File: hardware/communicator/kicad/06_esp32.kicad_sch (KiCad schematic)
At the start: 5 parts, among them U11 ESP32-S3-MINI-1-N4R2

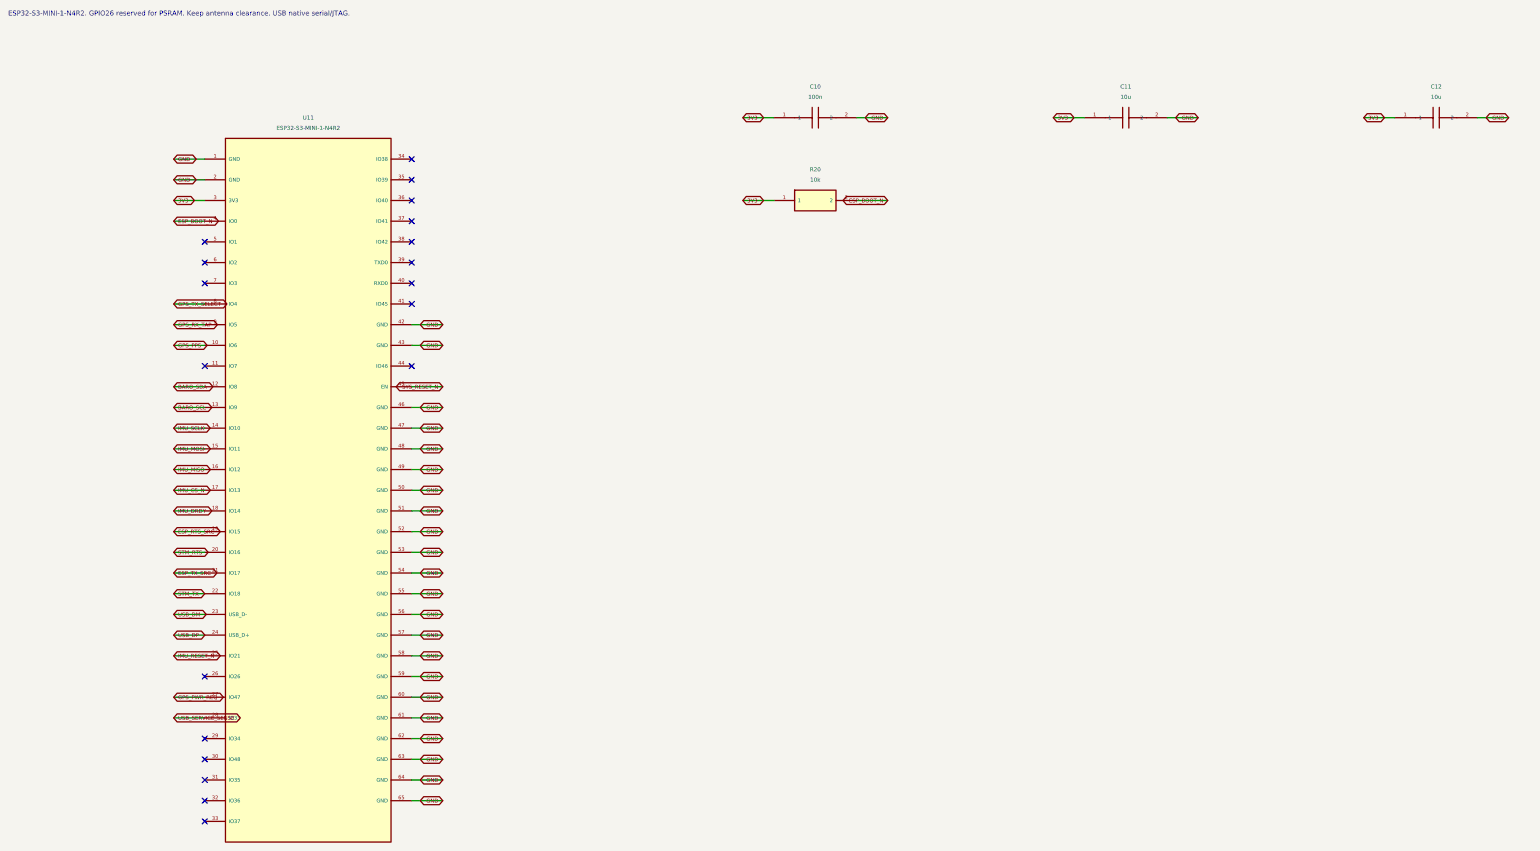
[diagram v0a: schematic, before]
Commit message: feat: add R1 detailed hardware and navigation protocol review candidate
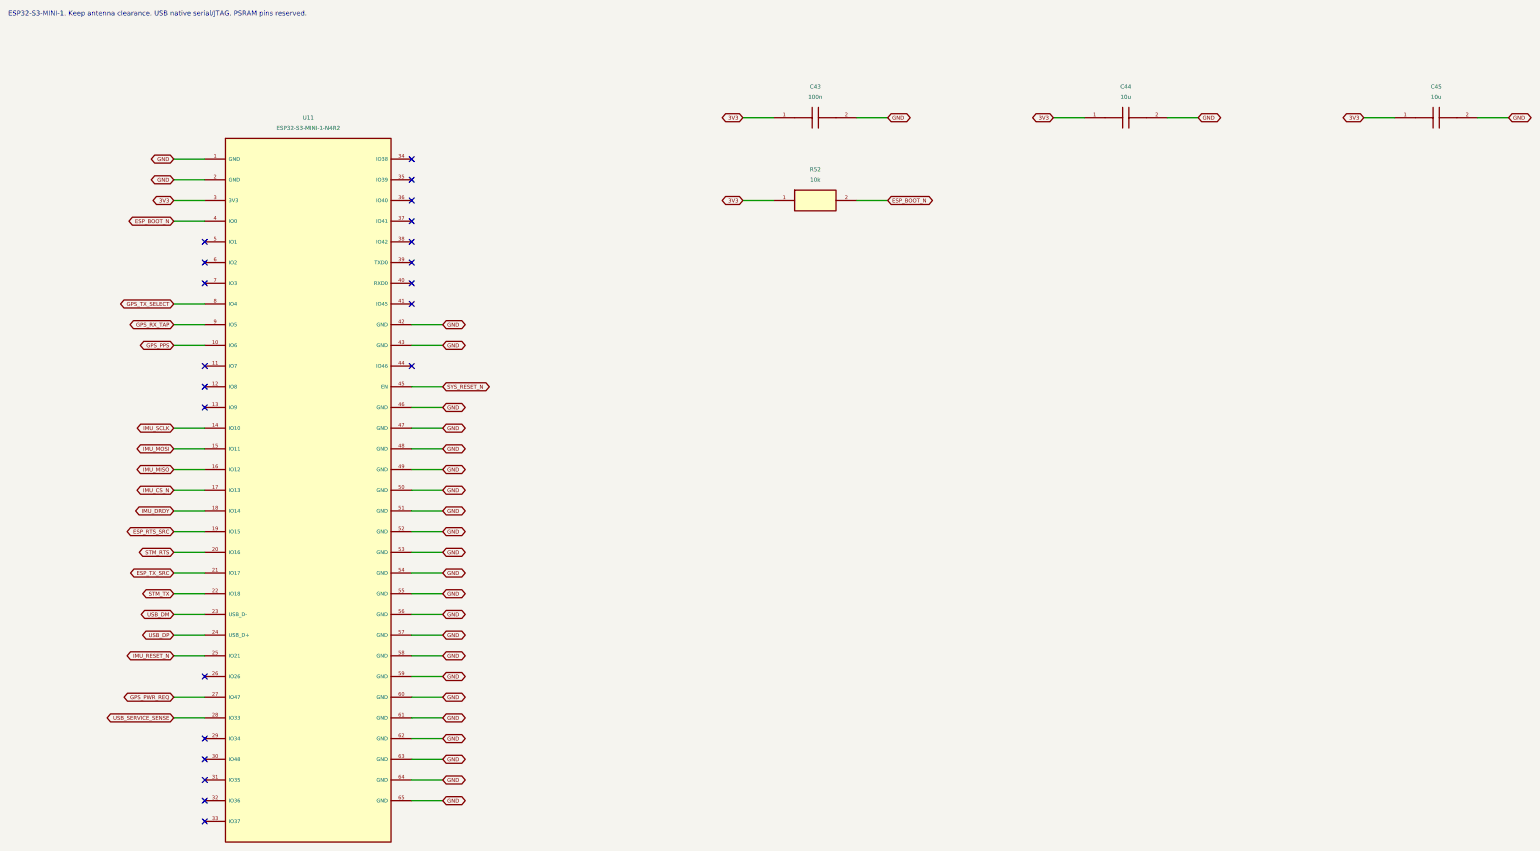
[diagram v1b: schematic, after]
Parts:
- removed C10: 100n, CANView:Capacitor_SMD__C_0603_1608Metric, symbol CANView:CANView_communicator_C10
- removed C11: 10u, CANView:Capacitor_SMD__C_0603_1608Metric, symbol CANView:CANView_communicator_C11
- removed C12: 10u, CANView:Capacitor_SMD__C_0603_1608Metric, symbol CANView:CANView_communicator_C12
- removed R20: 10k, CANView:Resistor_SMD__R_0402_1005Metric, symbol CANView:CANView_communicator_R20
- added C43: 100n, CANView:Capacitor_SMD__C_0603_1608Metric, symbol CANView:CANView_communicator_C43
- added C44: 10u, CANView:Capacitor_SMD__C_0603_1608Metric, symbol CANView:CANView_communicator_C44
- added C45: 10u, CANView:Capacitor_SMD__C_0603_1608Metric, symbol CANView:CANView_communicator_C45
- added R52: 10k, CANView:Resistor_SMD__R_0402_1005Metric, symbol CANView:CANView_communicator_R52
- U11: footprint CANView:RF_Module__ESP32-S2-MINI-1 -> CANView:ESP32-S3-MINI-1; Source esp32s3-mini: pin table, peripheral schematic and land patt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 -> esp32s3-mini
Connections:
- net 3V3: now also C43.1, C44.1, C45.1, R52.1
- net ESP_BOOT_N: now also R52.2
- net GND: now also C43.2, C44.2, C45.2
- net BARO_SCL: no longer names the net of U11.13 (IO9)
- net BARO_SDA: no longer names the net of U11.12 (IO8)
- no-connect marks 19 -> 21
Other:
- note added: "ESP32-S3-MINI-1. Keep antenna clearance. USB native serial/JTAG. PSRAM pins reserved."
- note removed: "ESP32-S3-MINI-1-N4R2. GPIO26 reserved for PSRAM. Keep antenna clearance. USB native serial/JTAG."

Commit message: fix: close hardware rail-fault paths and sensor contract gaps
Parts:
- removed C43: 100n, CANView:Capacitor_SMD__C_0603_1608Metric, symbol CANView:CANView_communicator_C43
- removed C44: 10u, CANView:Capacitor_SMD__C_0603_1608Metric, symbol CANView:CANView_communicator_C44
- removed R52: 10k, CANView:Resistor_SMD__R_0402_1005Metric, symbol CANView:CANView_communicator_R52
- added C46: 10u, CANView:Capacitor_SMD__C_0603_1608Metric, symbol CANView:CANView_communicator_C46
- added C47: 10u, CANView:Capacitor_SMD__C_0603_1608Metric, symbol CANView:CANView_communicator_C47
- added R53: 10k, CANView:Resistor_SMD__R_0402_1005Metric, symbol CANView:CANView_communicator_R53
- C45: value 10u -> 100n; MPN GEN-C-0603-10u-16V-X7R -> GEN-C-0603-100n-16V-X7R
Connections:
- net 3V3: now also C46.1, C47.1, R53.1
- net ESP_BOOT_N: now also R53.2
- net GND: now also C46.2, C47.2
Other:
- moved on the sheet: C45

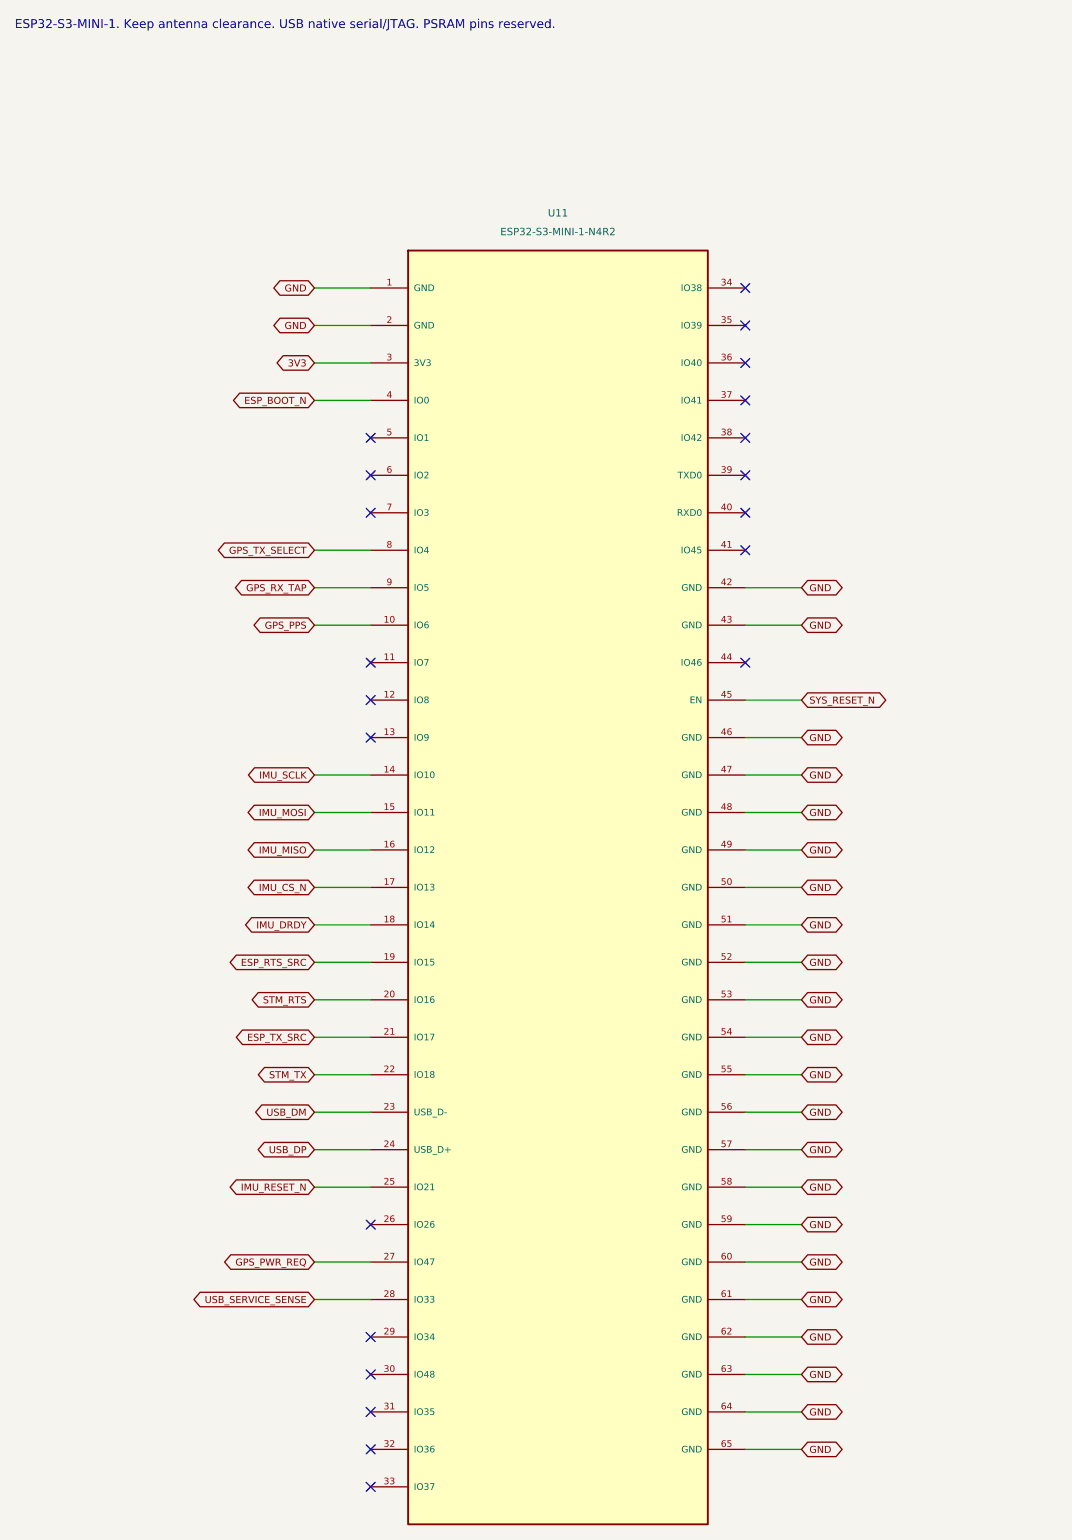
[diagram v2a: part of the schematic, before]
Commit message: Design independent OTA recovery and update N16R8 hardware
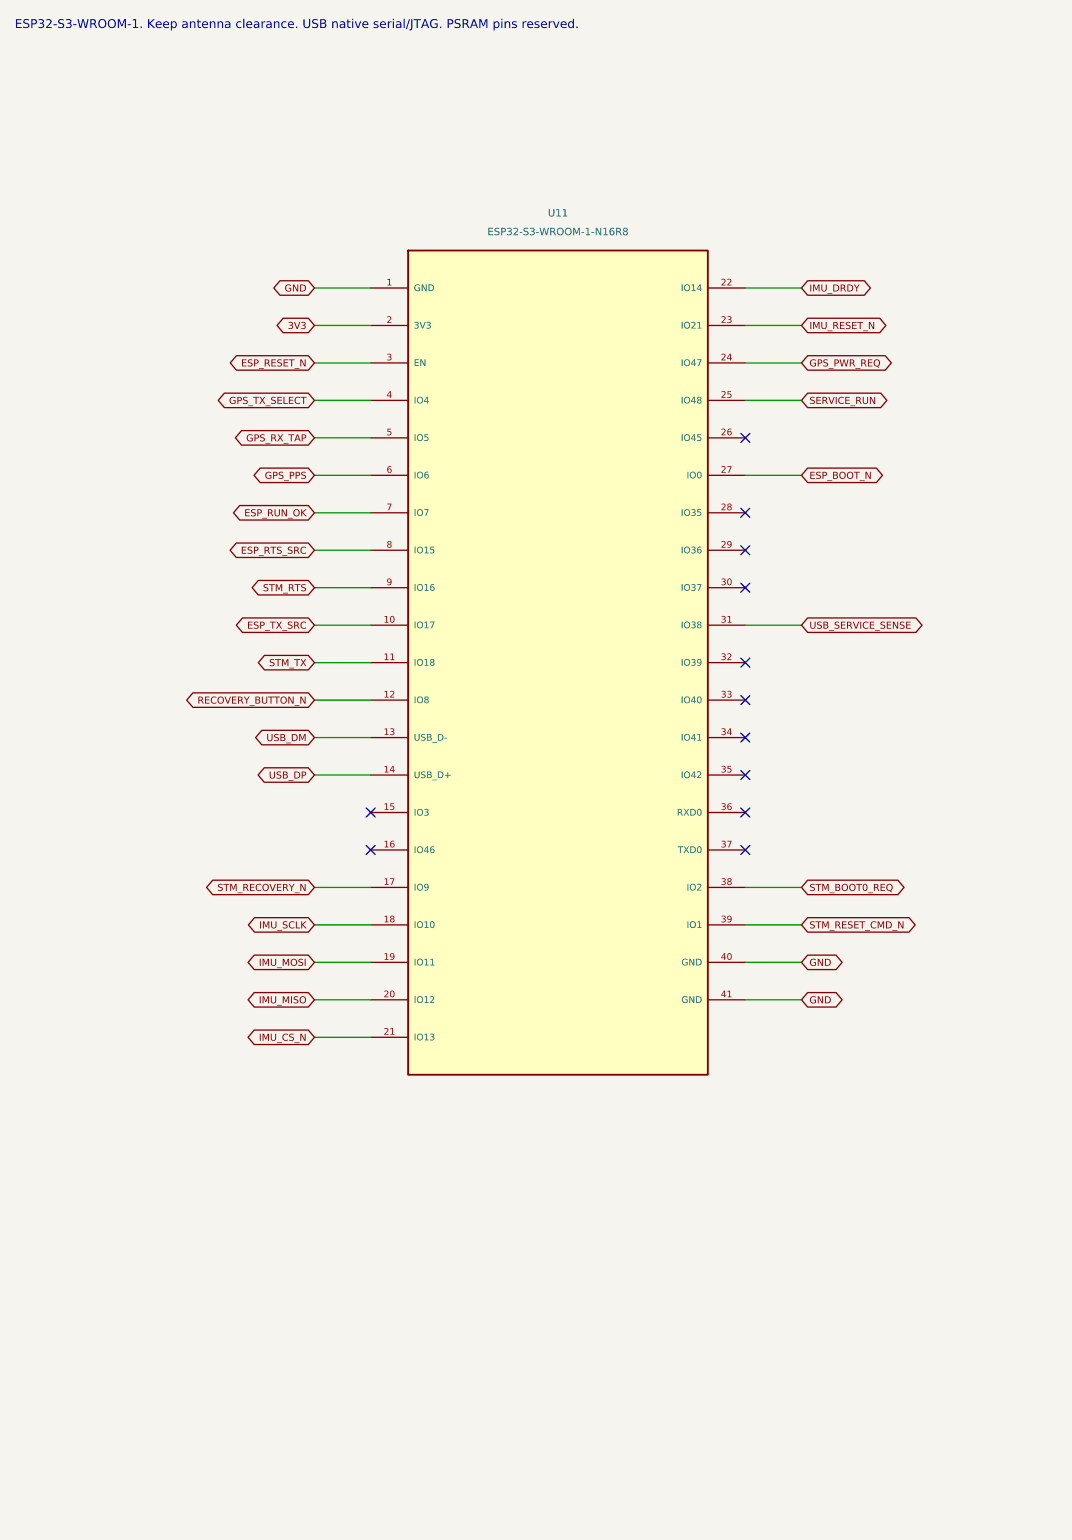
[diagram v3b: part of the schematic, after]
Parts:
- U11: value ESP32-S3-MINI-1-N4R2 -> ESP32-S3-WROOM-1-N16R8; footprint CANView:ESP32-S3-MINI-1 -> CANView:RF_Module__ESP32-S3-WROOM-1; MPN ESP32-S3-MINI-1-N4R2 -> ESP32-S3-WROOM-1-N16R8; Source esp32s3-mini -> esp32s3-wroom: ordering table, pin definitions, R8 reserved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; Specification 4MB flash + 2MB PSRAM; 3.0..3.6V; -40..85C -> 16MiB Quad flash + 8MiB Octal PSRAM; 3.0..3.6V; -40..65C ba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
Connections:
- net 3V3: now also U11.2 (3V3); no longer U11.3 (3V3)
- net ESP_BOOT_N: now also U11.27 (IO0); no longer U11.4 (IO0)
- net ESP_RTS_SRC: now also U11.8 (IO15); no longer U11.19 (IO15)
- net ESP_TX_SRC: now also U11.10 (IO17); no longer U11.21 (IO17)
- net GND: now also U11.40 (GND), U11.41 (GND); no longer U11.2 (GND), U11.42 (GND), U11.43 (GND), U11.46 (GND), U11.47 (GND), U11.48 (GND), U11.49 (GND), U11.50 (GND), U11.51 (GND), U11.52 (GND), U11.53 (GND), U11.54 (GND), U11.55 (GND), U11.56 (GND), U11.57 (GND), U11.58 (GND), U11.59 (GND), U11.60 (GND), U11.61 (GND), U11.62 (GND), U11.63 (GND), U11.64 (GND), U11.65 (GND)
- net GPS_PPS: now also U11.6 (IO6); no longer U11.10 (IO6)
- net GPS_PWR_REQ: now also U11.24 (IO47); no longer U11.27 (IO47)
- net GPS_RX_TAP: now also U11.5 (IO5); no longer U11.9 (IO5)
- net GPS_TX_SELECT: now also U11.4 (IO4); no longer U11.8 (IO4)
- net IMU_CS_N: now also U11.21 (IO13); no longer U11.17 (IO13)
- net IMU_DRDY: now also U11.22 (IO14); no longer U11.18 (IO14)
- net IMU_MISO: now also U11.20 (IO12); no longer U11.16 (IO12)
- net IMU_MOSI: now also U11.19 (IO11); no longer U11.15 (IO11)
- net IMU_RESET_N: now also U11.23 (IO21); no longer U11.25 (IO21)
- net IMU_SCLK: now also U11.18 (IO10); no longer U11.14 (IO10)
- net STM_RTS: now also U11.9 (IO16); no longer U11.20 (IO16)
- net STM_TX: now also U11.11 (IO18); no longer U11.22 (IO18)
- net USB_DM: now also U11.13 (USB_D-); no longer U11.23 (USB_D-)
- net USB_DP: now also U11.14 (USB_D+); no longer U11.24 (USB_D+)
- net USB_SERVICE_SENSE: now also U11.31 (IO38); no longer U11.28 (IO33)
- net RECOVERY_BUTTON_N: now reaches U11.12 (IO8)
- net STM_BOOT0_REQ: now reaches U11.38 (IO2)
- net STM_RESET_CMD_N: now reaches U11.39 (IO1)
- net ESP_RUN_OK: now reaches U11.7 (IO7)
- removed net SYS_RESET_N: U11.45 (EN)
- new net ESP_RESET_N: U11.3 (EN)
- new net SERVICE_RUN: U11.25 (IO48)
- new net STM_RECOVERY_N: U11.17 (IO9)
- no-connect marks 21 -> 12
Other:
- note added: "ESP32-S3-WROOM-1. Keep antenna clearance. USB native serial/JTAG. PSRAM pins reserved."
- note removed: "ESP32-S3-MINI-1. Keep antenna clearance. USB native serial/JTAG. PSRAM pins reserved."

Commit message: Fix OTA service interlock and durable activation policy
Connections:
- net SERVICE_RUN renamed SERVICE_RUN_SENSE
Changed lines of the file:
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@@
-(kicad_sch (version 20250114) (generator "eeschema") (generator_version "10.0") (paper "A3") (title_block (title "CANView / 06_esp32") (date "2026-09-05") (rev "R1 REVIEW") (company "digitie/canview") (comment 1 "SCHEMATIC REVIEW ONLY - PCB/HIL release gates remain open"))
+(kicad_sch (version 20250114) (generator "eeschema") (generator_version "10.0") (paper "A3") (title_block (title "CANView / 06_esp32") (date "2026-09-06") (rev "R2 N16R8 REVIEW") (company "digitie/canview") (comment 1 "SCHEMATIC REVIEW ONLY - PCB/HIL release gates remain open"))
 (text "ESP32-S3-WROOM-1. Keep antenna clearance. USB native serial/JTAG. PSRAM pins reserved." (at 15.24 15.24 0) (effects (font (size 1.2 1.2)) (justify left)))
 (symbol (lib_id "CANView:CANView_communicator_U11") (at 88.9000 101.6000 0) (unit 1) (in_bom yes) (on_board yes) (dnp no) (property "Reference" "U11" (at 88.9000 40.6400 0)  (effects (font (size 1.0 1.0)) ))(property "Value" "ESP32-S3-WROOM-1-N16R8" (at 88.9000 43.1800 0)  (effects (font (size 1.0 1.0)) ))(property "Footprint" "CANView:RF_Module__ESP32-S3-WROOM-1" (at 88.9000 101.6000 0) (hide yes) (effects (font (size 1.0 1.0)) ))(property "MPN" "ESP32-S3-WROOM-1-N16R8" (at 88.9000 101.6000 0) (hide yes) (effects (font (size 1.0 1.0)) ))(property "Specification" "16MiB Quad flash + 8MiB Octal PSRAM; 3.0..3.6V; -40..65C base, up to85C with PSRAM ECC; ECC usable7.5MiB; validate complete board thermal range" (at 88.9000 101.6000 0) (hide yes) (effects (font (size 1.0 1.0)) ))(property "Source" "esp32s3-wroom: ordering table, pin definitions, R8 reserved GPIO35/36/37; PSRAM ECC temperature note" (at 88.9000 101.6000 0) (hide yes) (effects (font (size 1.0 1.0)) ))(property "Assembly" "FIT" (at 88.9000 101.6000 0) (hide yes) (effects (font (size 1.0 1.0)) ))(instances (project "communicator" (path "/c8ff26d1-0b80-520e-ae3f-45aa29bfe092/7d2a19a8-f6e3-55c6-b2b0-a8300957e8c4" (reference "U11") (unit 1)))))
@@
 (global_label "GPS_PWR_REQ" (shape bidirectional) (at 121.9200 60.9600 0) (effects (font (size 0.95 0.95)) (justify left)) (property "Intersheetrefs" "${INTERSHEET_REFS}" (at 121.9200 60.9600 0) (hide yes) (effects (font (size 1.0 1.0)) )))
 (wire (pts (xy 114.3000 66.0400) (xy 121.9200 66.0400)) (stroke (width 0) (type default)))
-(global_label "SERVICE_RUN" (shape bidirectional) (at 121.9200 66.0400 0) (effects (font (size 0.95 0.95)) (justify left)) (property "Intersheetrefs" "${INTERSHEET_REFS}" (at 121.9200 66.0400 0) (hide yes) (effects (font (size 1.0 1.0)) )))
+(global_label "SERVICE_RUN_SENSE" (shape bidirectional) (at 121.9200 66.0400 0) (effects (font (size 0.95 0.95)) (justify left)) (property "Intersheetrefs" "${INTERSHEET_REFS}" (at 121.9200 66.0400 0) (hide yes) (effects (font (size 1.0 1.0)) )))
 (no_connect (at 114.3000 71.1200))
 (wire (pts (xy 114.3000 76.2000) (xy 121.9200 76.2000)) (stroke (width 0) (type default)))
